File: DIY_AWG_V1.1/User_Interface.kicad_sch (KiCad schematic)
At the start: 28 parts, among them SW10 SW_Push, SW11 SW_Push, SW12 SW_Push, SW13 SW_Push, SW14 SW_Push, SW15 SW_Push, SW16 SW_Push, SW17 SW_Push, SW18 SW_Push, SW19 SW_Push, SW20 SW_Push, SW21 SW_Push, SW22 SW_Push, SW23 SW_Push, SW3 SW_Push, SW4 SW_Push, SW5 SW_Push, SW6 SW_Push, SW7 SW_Push, SW8 SW_Push, SW9 SW_Push, U1 EC12D1564402, U5 EC12E2430404

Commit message: Updated AD9834_DDS, amplifier, STM32_MCU schematic
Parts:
- renumbered C13 to C60, D2 to D1, D4 to D2, D5 to D4, SW4 to SW10, SW7 to SW11, SW10 to SW12, SW16 to SW14, SW19 to SW15, SW22 to SW16, SW5 to SW17, SW8 to SW18, SW11 to SW19, SW14 to SW20, SW17 to SW21, SW20 to SW22, SW6 to SW4, SW9 to SW5, SW12 to SW6, SW15 to SW7, SW18 to SW8, SW21 to SW9, U1 to U13, U5 to U14

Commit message: Updated STM32_MCU, amplifier, User_Interface, AD9834_DDS schematic
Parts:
- renumbered C60 to C73, U13 to U14, U14 to U15
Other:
- note added: "100nF MLCC (1): C0603C104J3RACTU (1)"
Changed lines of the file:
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@@
 		)
 	)
+	(text "100nF MLCC (1): C0603C104J3RACTU (1)"
+		(exclude_from_sim no)
+		(at 196.596 20.32 0)
+		(effects
+			(font
+				(size 1.27 1.27)
+			)
+		)
+	)
 	(text "MH1, MH2 are Mounting Pads"
 		(exclude_from_sim no)
@@
 		(dnp no)
 		(fields_autoplaced yes)
-		(property "Reference" "#PWR0123"
+		(property "Reference" "#PWR0135"
 			(at 20.32 78.74 0)
 			(hide yes)
@@
 			(project "DIY_AWG_V1.1"
 				(path "/508078af-d961-4af3-840e-a064a9f8d5bc/5e4867af-4e97-464f-8d5d-dfa2d7b207c5"
-					(reference "#PWR0123")
+					(reference "#PWR0135")
 					(unit 1)
 				)
@@
 		(dnp no)
 		(fields_autoplaced yes)
-		(property "Reference" "#PWR0128"
+		(property "Reference" "#PWR0140"
 			(at 73.66 86.36 0)
 			(hide yes)
@@
 			(project "DIY_AWG_V1.1"
 				(path "/508078af-d961-4af3-840e-a064a9f8d5bc/5e4867af-4e97-464f-8d5d-dfa2d7b207c5"
-					(reference "#PWR0128")
+					(reference "#PWR0140")
 					(unit 1)
 				)
@@
 		(dnp no)
 		(fields_autoplaced yes)
-		(property "Reference" "#PWR0125"
+		(property "Reference" "#PWR0137"
 			(at 62.23 76.2 0)
 			(hide yes)
@@
 			(project "DIY_AWG_V1.1"
 				(path "/508078af-d961-4af3-840e-a064a9f8d5bc/5e4867af-4e97-464f-8d5d-dfa2d7b207c5"
-					(reference "#PWR0125")
+					(reference "#PWR0137")
 					(unit 1)
 				)
@@
 		(dnp no)
 		(fields_autoplaced yes)
-		(property "Reference" "#PWR0127"
+		(property "Reference" "#PWR0139"
 			(at 73.66 50.8 0)
 			(hide yes)
@@
 			(project "DIY_AWG_V1.1"
 				(path "/508078af-d961-4af3-840e-a064a9f8d5bc/5e4867af-4e97-464f-8d5d-dfa2d7b207c5"
-					(reference "#PWR0127")
+					(reference "#PWR0139")
 					(unit 1)
 				)
@@
 		(dnp no)
 		(fields_autoplaced yes)
-		(property "Reference" "#PWR0131"
+		(property "Reference" "#PWR0143"
 			(at 125.73 50.8 0)
 			(hide yes)
@@
 			(project "DIY_AWG_V1.1"
 				(path "/508078af-d961-4af3-840e-a064a9f8d5bc/5e4867af-4e97-464f-8d5d-dfa2d7b207c5"
-					(reference "#PWR0131")
+					(reference "#PWR0143")
 					(unit 1)
 				)
@@
 		(dnp no)
 		(fields_autoplaced yes)
-		(property "Reference" "#PWR0133"
+		(property "Reference" "#PWR0145"
 			(at 166.37 50.8 0)
 			(hide yes)
@@
 			(project "DIY_AWG_V1.1"
 				(path "/508078af-d961-4af3-840e-a064a9f8d5bc/5e4867af-4e97-464f-8d5d-dfa2d7b207c5"
-					(reference "#PWR0133")
+					(reference "#PWR0145")
 					(unit 1)
 				)
@@
 		(dnp no)
 		(fields_autoplaced yes)
-		(property "Reference" "#PWR0132"
+		(property "Reference" "#PWR0144"
 			(at 125.73 86.36 0)
 			(hide yes)
@@
 			(project "DIY_AWG_V1.1"
 				(path "/508078af-d961-4af3-840e-a064a9f8d5bc/5e4867af-4e97-464f-8d5d-dfa2d7b207c5"
-					(reference "#PWR0132")
+					(reference "#PWR0144")
 					(unit 1)
 				)
@@
 		(in_pos_files yes)
 		(dnp no)
-		(property "Reference" "U14"
+		(property "Reference" "U15"
 			(at 45.72 61.976 0)
 			(show_name no)
@@
 			(project "DIY_AWG_V1.1"
 				(path "/508078af-d961-4af3-840e-a064a9f8d5bc/5e4867af-4e97-464f-8d5d-dfa2d7b207c5"
-					(reference "U14")
+					(reference "U15")
 					(unit 1)
 				)
@@
 		(dnp no)
 		(fields_autoplaced yes)
-		(property "Reference" "#PWR0134"
+		(property "Reference" "#PWR0146"
 			(at 166.37 86.36 0)
 			(hide yes)
@@
 			(project "DIY_AWG_V1.1"
 				(path "/508078af-d961-4af3-840e-a064a9f8d5bc/5e4867af-4e97-464f-8d5d-dfa2d7b207c5"
-					(reference "#PWR0134")
+					(reference "#PWR0146")
 					(unit 1)
 				)
@@
 		(in_pos_files yes)
 		(dnp no)
-		(property "Reference" "U13"
+		(property "Reference" "U14"
 			(at 45.72 21.336 0)
 			(show_name no)
@@
 			(project "DIY_AWG_V1.1"
 				(path "/508078af-d961-4af3-840e-a064a9f8d5bc/5e4867af-4e97-464f-8d5d-dfa2d7b207c5"
-					(reference "U13")
+					(reference "U14")
 					(unit 1)
 				)
@@
 		(dnp no)
 		(fields_autoplaced yes)
-		(property "Reference" "#PWR0130"
+		(property "Reference" "#PWR0142"
 			(at 114.3 86.36 0)
 			(hide yes)
@@
 			(project "DIY_AWG_V1.1"
 				(path "/508078af-d961-4af3-840e-a064a9f8d5bc/5e4867af-4e97-464f-8d5d-dfa2d7b207c5"
-					(reference "#PWR0130")
+					(reference "#PWR0142")
 					(unit 1)
 				)
@@
 		(dnp no)
 		(fields_autoplaced yes)
-		(property "Reference" "#PWR0124"
+		(property "Reference" "#PWR0136"
 			(at 31.75 52.07 0)
 			(hide yes)
@@
 			(project "DIY_AWG_V1.1"
 				(path "/508078af-d961-4af3-840e-a064a9f8d5bc/5e4867af-4e97-464f-8d5d-dfa2d7b207c5"
-					(reference "#PWR0124")
+					(reference "#PWR0136")
 					(unit 1)
 				)
@@
 		(dnp no)
 		(fields_autoplaced yes)
-		(property "Reference" "#PWR0129"
+		(property "Reference" "#PWR0141"
 			(at 114.3 50.8 0)
 			(hide yes)
@@
 			(project "DIY_AWG_V1.1"
 				(path "/508078af-d961-4af3-840e-a064a9f8d5bc/5e4867af-4e97-464f-8d5d-dfa2d7b207c5"
-					(reference "#PWR0129")
+					(reference "#PWR0141")
 					(unit 1)
 				)
@@
 		(in_pos_files yes)
 		(dnp no)
-		(property "Reference" "C60"
+		(property "Reference" "C73"
 			(at 29.21 39.37 0)
 			(show_name no)
@@
 			(project "DIY_AWG_V1.1"
 				(path "/508078af-d961-4af3-840e-a064a9f8d5bc/5e4867af-4e97-464f-8d5d-dfa2d7b207c5"
-					(reference "C60")
+					(reference "C73")
 					(unit 1)
 				)
@@
 		(dnp no)
 		(fields_autoplaced yes)
-		(property "Reference" "#PWR0122"
+		(property "Reference" "#PWR0134"
 			(at 20.32 40.64 0)
 			(hide yes)
@@
 			(project "DIY_AWG_V1.1"
 				(path "/508078af-d961-4af3-840e-a064a9f8d5bc/5e4867af-4e97-464f-8d5d-dfa2d7b207c5"
-					(reference "#PWR0122")
+					(reference "#PWR0134")
 					(unit 1)
 				)
@@
 		(dnp no)
 		(fields_autoplaced yes)
-		(property "Reference" "#PWR0126"
+		(property "Reference" "#PWR0138"
 			(at 63.5 36.83 0)
 			(hide yes)
@@
 			(project "DIY_AWG_V1.1"
 				(path "/508078af-d961-4af3-840e-a064a9f8d5bc/5e4867af-4e97-464f-8d5d-dfa2d7b207c5"
-					(reference "#PWR0126")
+					(reference "#PWR0138")
 					(unit 1)
 				)

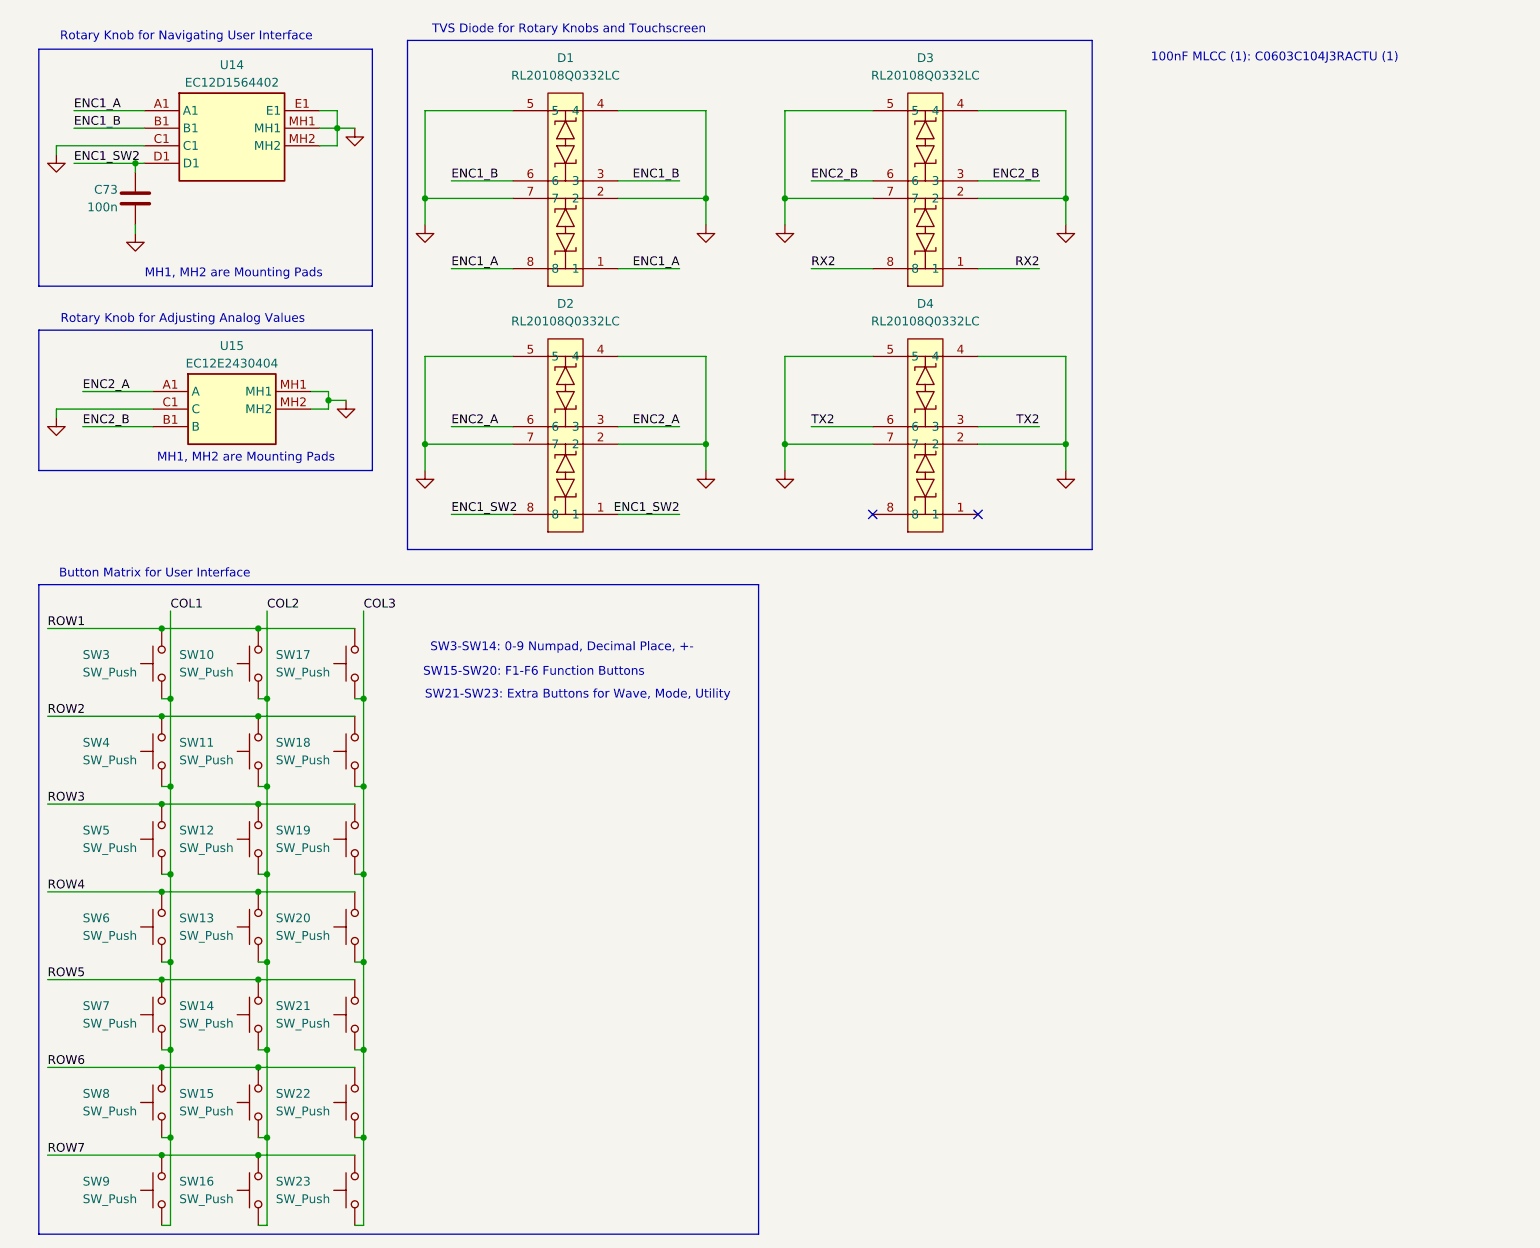
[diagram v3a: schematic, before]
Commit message: Updated pin description of relevant components
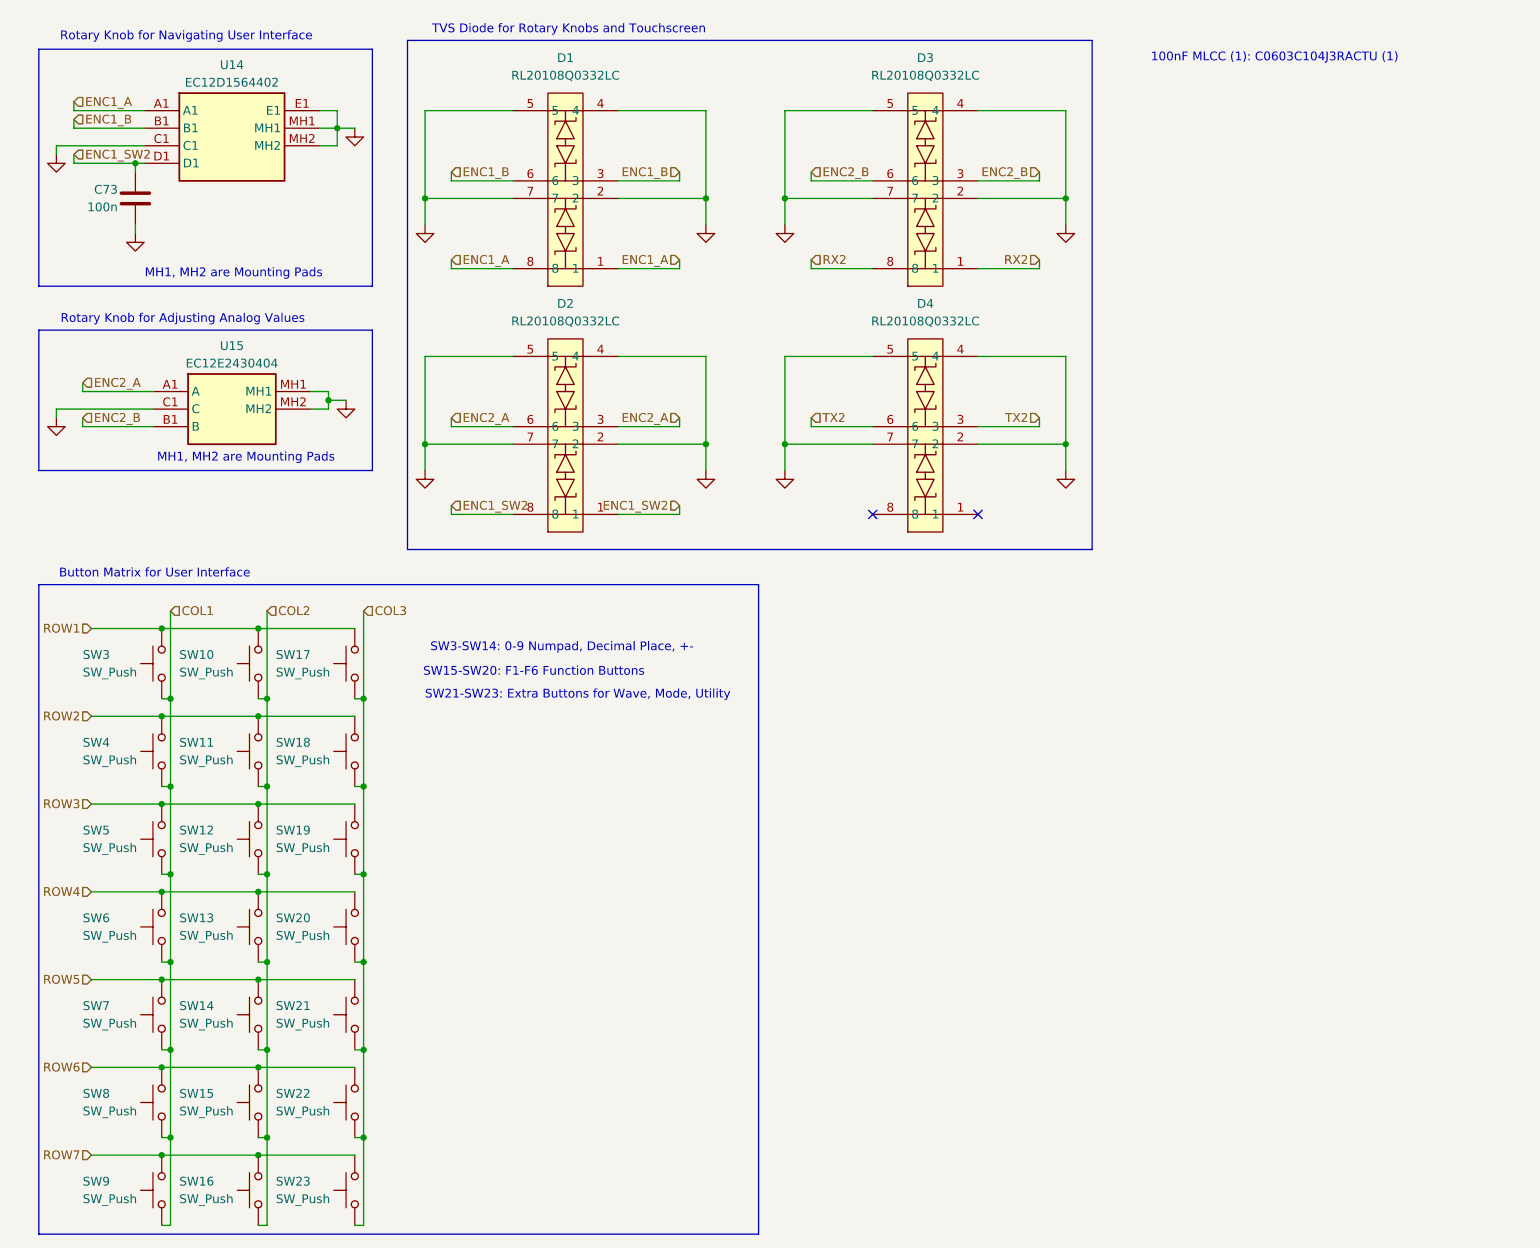
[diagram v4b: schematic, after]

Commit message: Updated schematics to clear ERCs
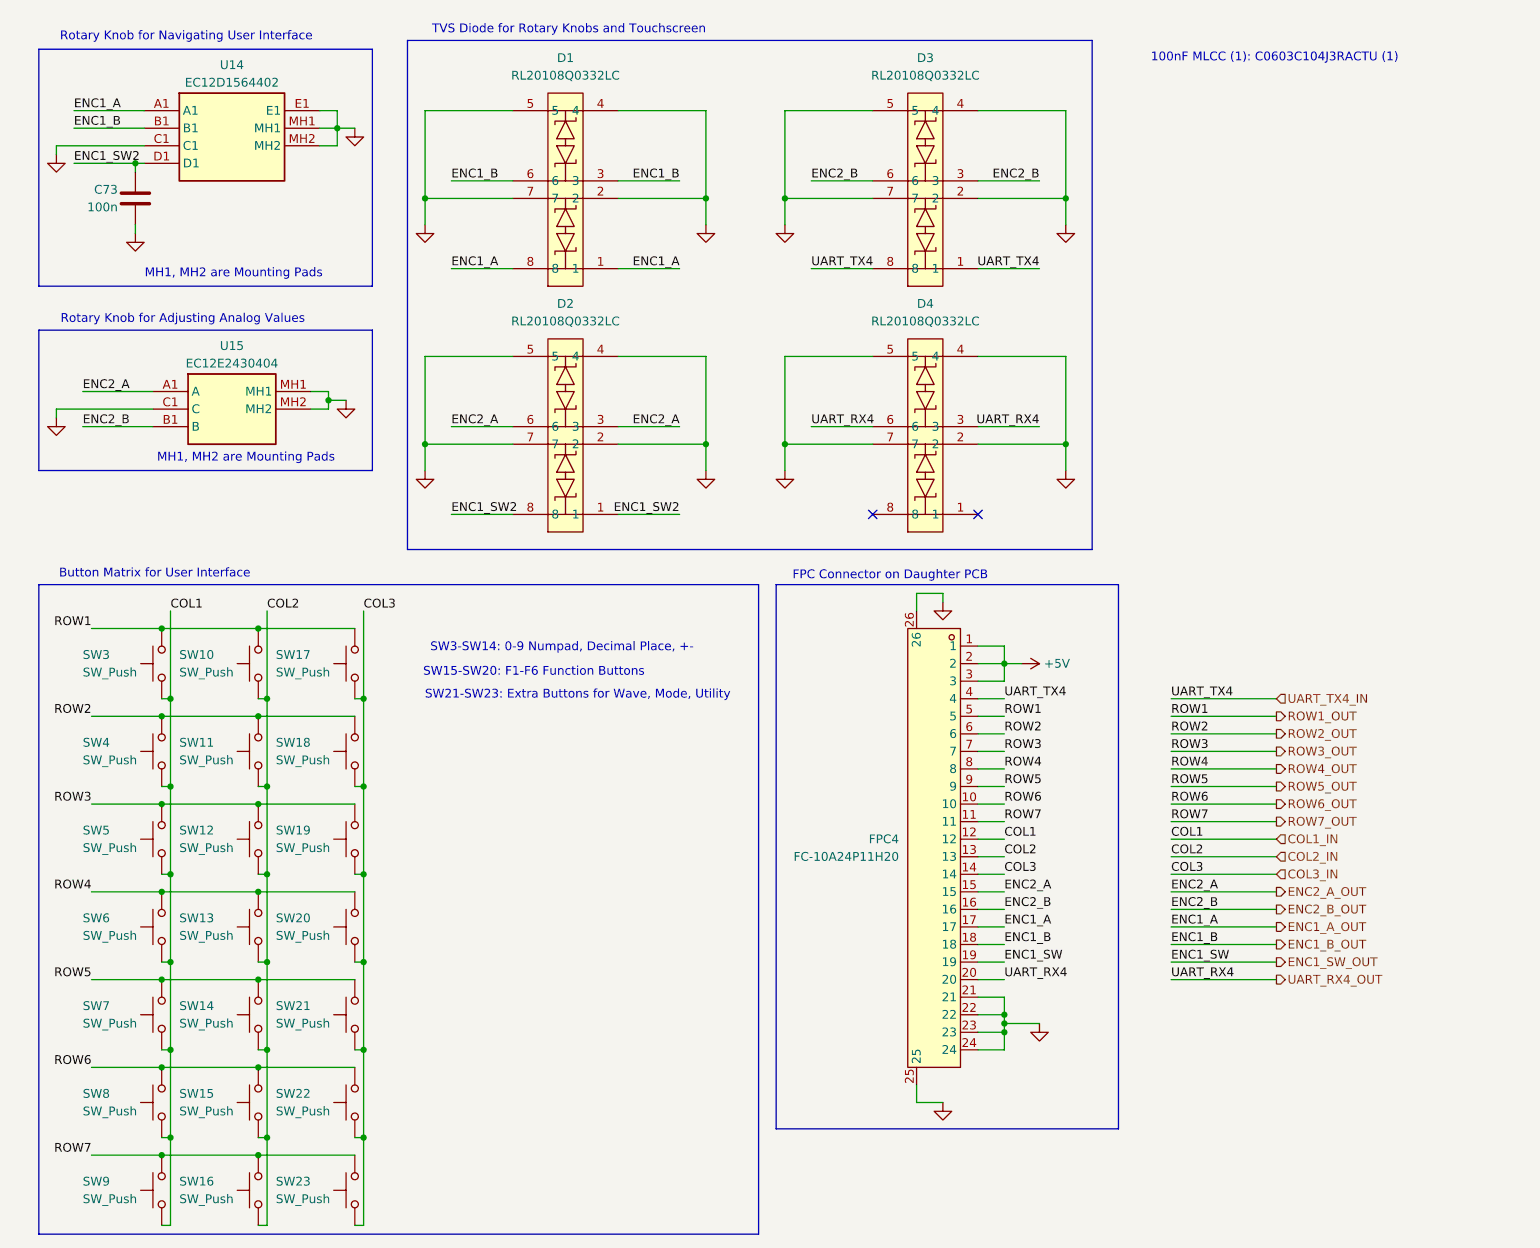
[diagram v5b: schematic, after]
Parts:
- added FPC4: FC-10A24P11H20, easyeda2kicad:FPC-SMD_24P-P1.00_FC-10A24P11H20, symbol easyeda2kicad:FC-10A24P11H20
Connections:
- net GND: now also FPC4.21, FPC4.22, FPC4.23, FPC4.24, FPC4.25, FPC4.26
- net COL1 renamed COL1_IN
- net COL1_IN: now also FPC4.12
- net COL2 renamed COL2_IN
- net COL2_IN: now also FPC4.13
- net COL3 renamed COL3_IN
- net COL3_IN: now also FPC4.14
- net ENC1_A renamed ENC1_A_OUT
- net ENC1_A_OUT: now also FPC4.17
- net ENC1_B renamed ENC1_B_OUT
- net ENC1_B_OUT: now also FPC4.18
- net ENC2_A renamed ENC2_A_OUT
- net ENC2_A_OUT: now also FPC4.15
- net ENC2_B renamed ENC2_B_OUT
- net ENC2_B_OUT: now also FPC4.16
- net ROW1 renamed ROW1_OUT
- net ROW1_OUT: now also FPC4.5
- net ROW2 renamed ROW2_OUT
- net ROW2_OUT: now also FPC4.6
- net ROW3 renamed ROW3_OUT
- net ROW3_OUT: now also FPC4.7
- net ROW4 renamed ROW4_OUT
- net ROW4_OUT: now also FPC4.8
- net ROW5 renamed ROW5_OUT
- net ROW5_OUT: now also FPC4.9
- net ROW6 renamed ROW6_OUT
- net ROW6_OUT: now also FPC4.10
- net ROW7 renamed ROW7_OUT
- net ROW7_OUT: now also FPC4.11
- net RX2 renamed UART_TX4_IN
- net UART_TX4_IN: now also FPC4.4
- net TX2 renamed UART_RX4_OUT
- net UART_RX4_OUT: now also FPC4.20
- new net +5V: FPC4.1, FPC4.2, FPC4.3
- new net ENC1_SW_OUT: FPC4.19
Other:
- note added: "FPC Connector on Daughter PCB"
